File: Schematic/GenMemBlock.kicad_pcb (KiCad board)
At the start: 4 copper layers, 99.6 x 66 mm, 39 parts, among them J1 MCU_HEADER, J2 ADDR_BUS, J3 DATA_BUS, J4 CART_A20, J5 CART_B10, J6 CART_B20, J7 CART_A10, P1 MD-CART-FINGERS-doragasu, U1 74HCT595, U10 74ACT16543DL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

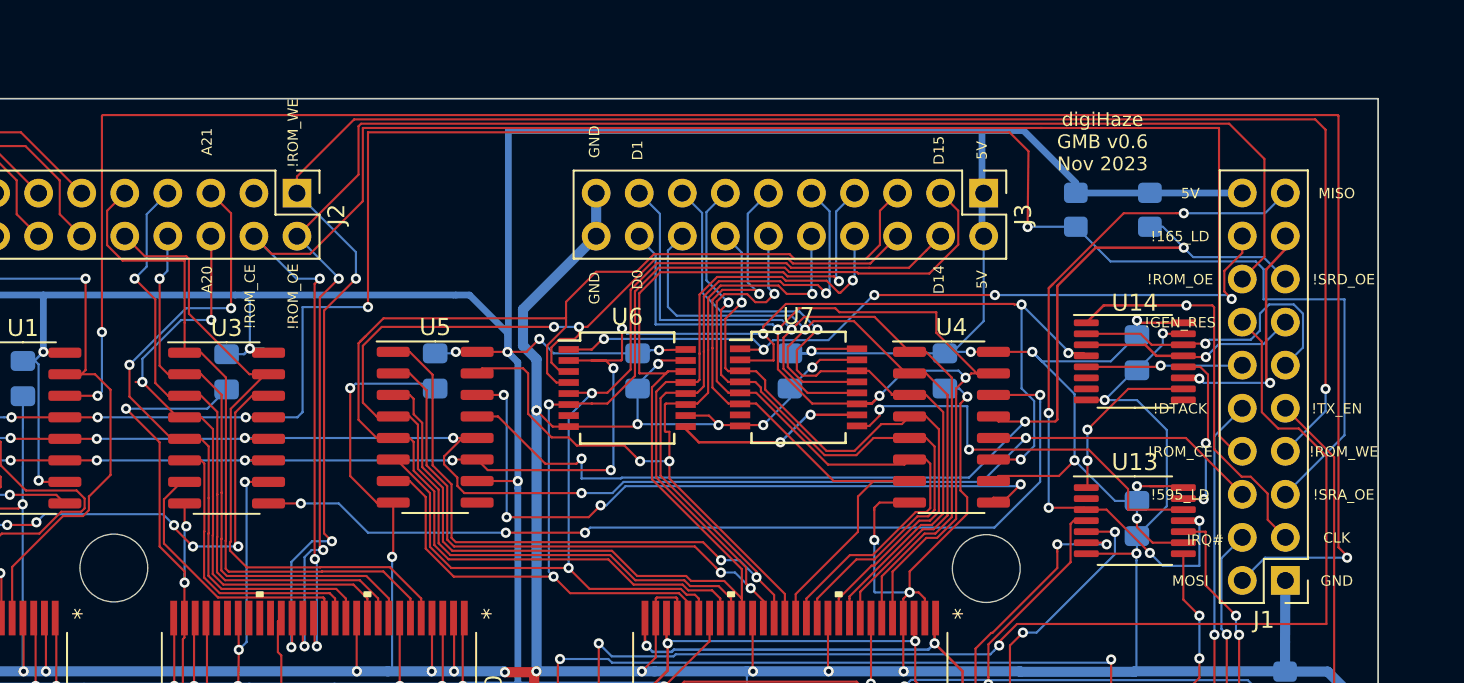
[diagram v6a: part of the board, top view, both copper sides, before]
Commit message: sdcard pinout
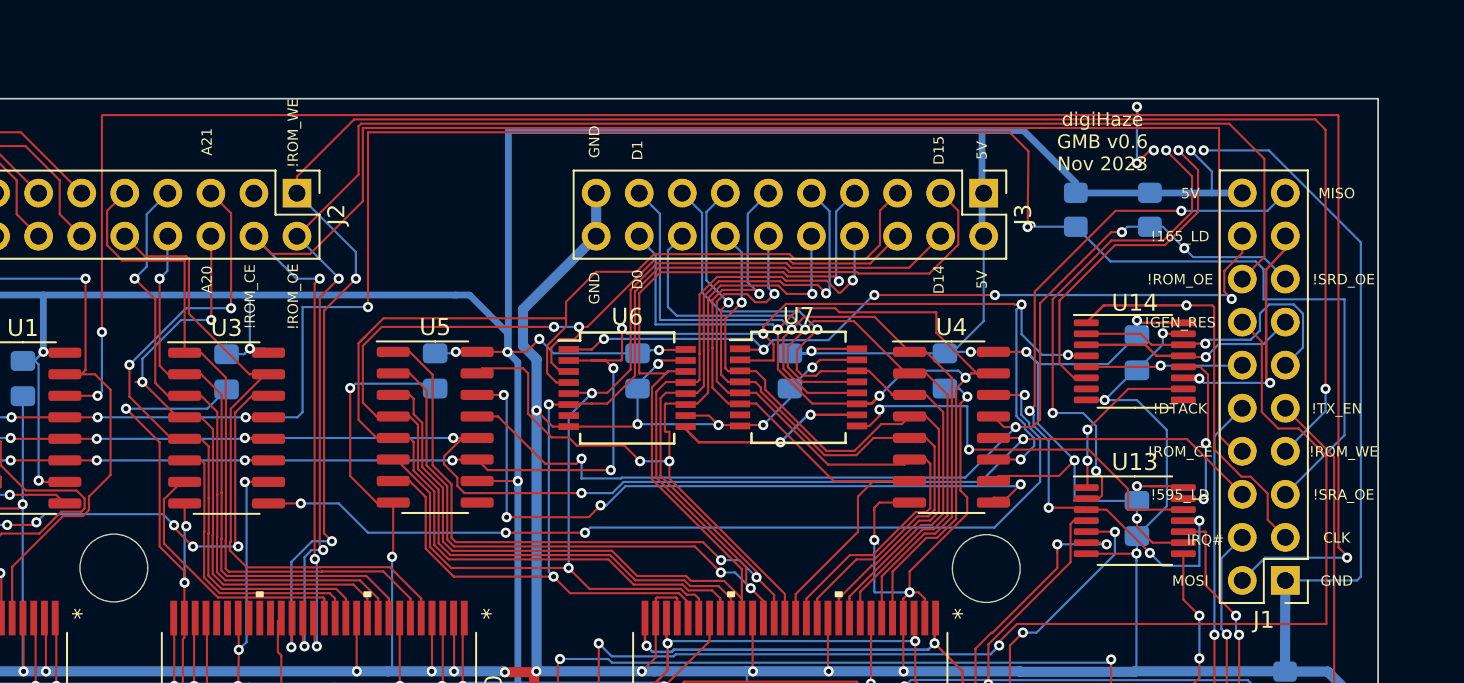
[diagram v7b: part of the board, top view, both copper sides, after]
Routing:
- net GND: track 646.6 -> 682.4 mm, vias 46 -> 47
- net SPI_MISO_SDC: track 0.00 -> 29.5 mm, vias 0 -> 3
- net CLK_SDC: track 0.00 -> 20.1 mm, vias 0 -> 1
- net /SER_MOSI: track 124.7 -> 129.8 mm, vias 3 -> 6
- net +5V: track 549.0 -> 553.7 mm, vias 40 -> 41
- net /595_DATA_OE#: track 65.6 -> 63.1 mm, vias 3 -> 4
- net MC_MISO: track 43.2 -> 44.5 mm
- net /SER_CLK: track 103.8 -> 105.0 mm

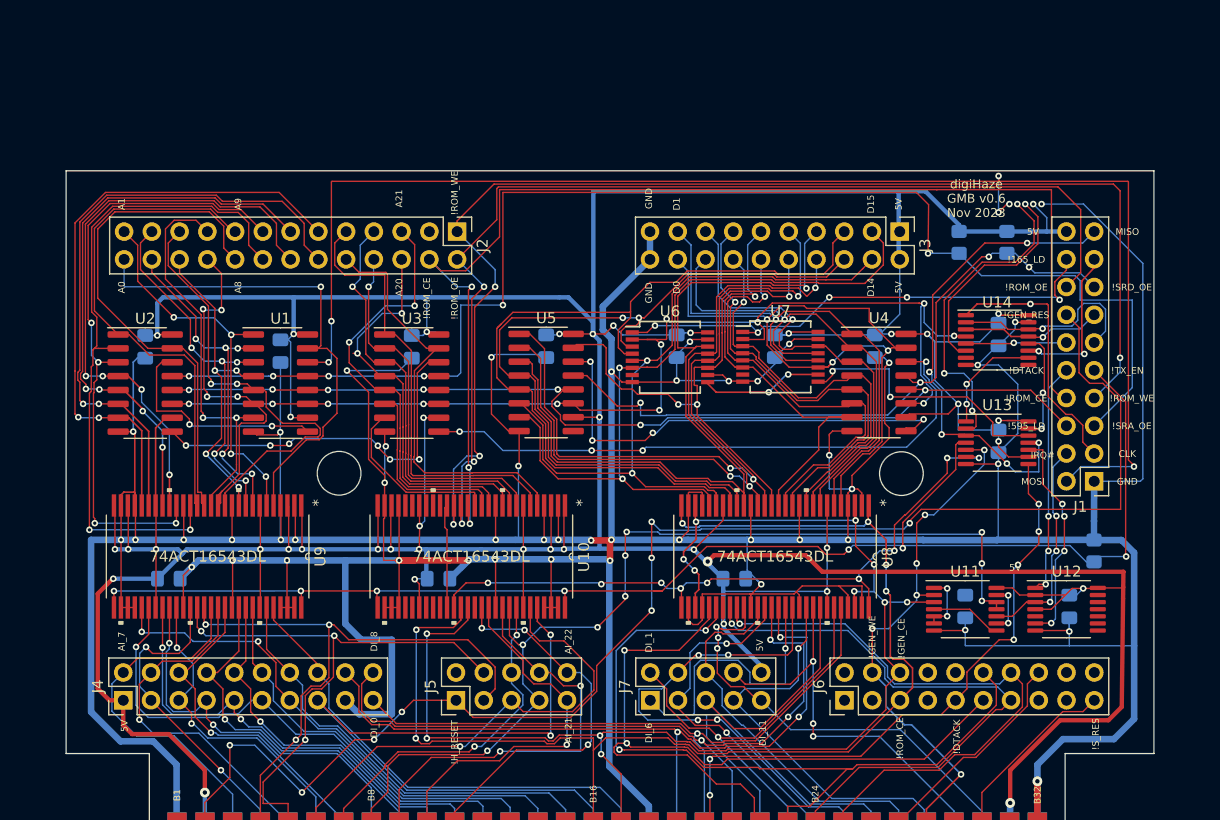
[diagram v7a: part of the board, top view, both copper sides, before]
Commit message: sdcard wiring
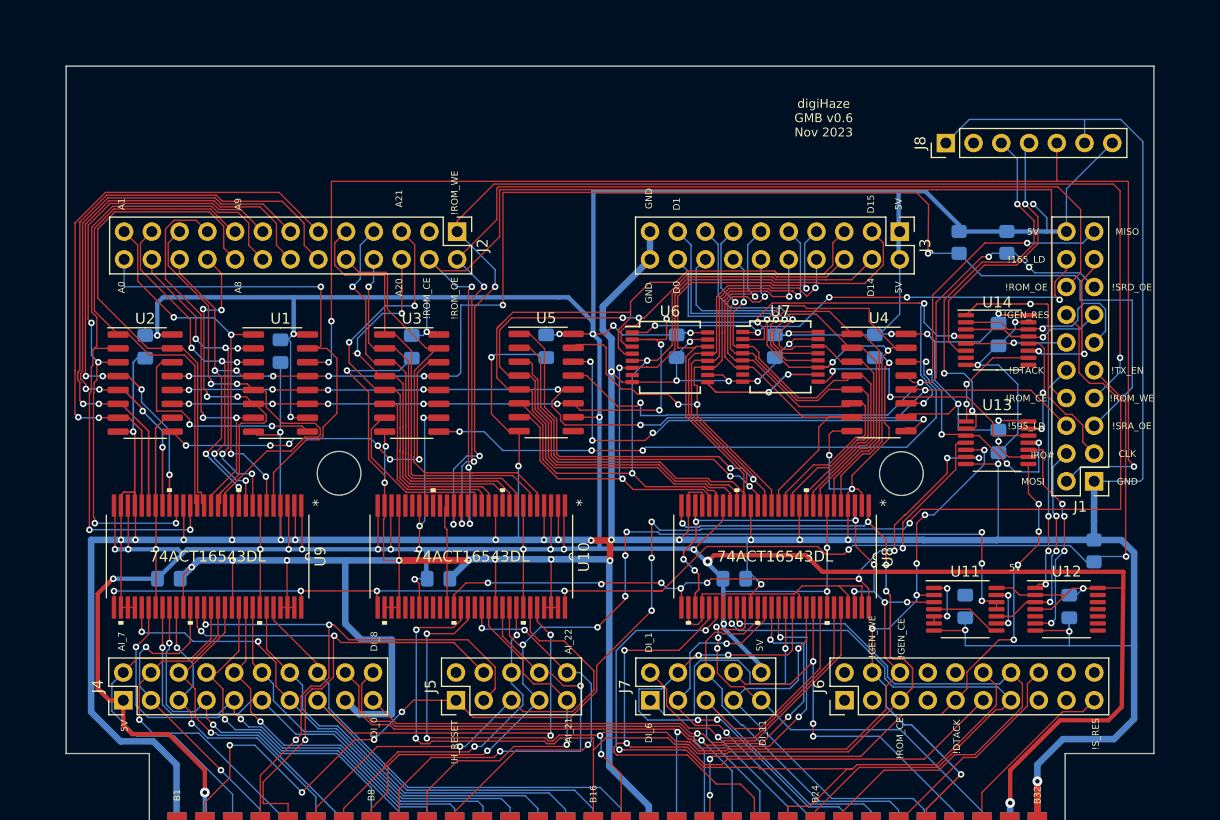
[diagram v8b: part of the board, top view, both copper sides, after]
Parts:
- added J8: SDCARD, Connector_PinHeader_2.54mm:PinHeader_1x07_P2.54mm_Vertical, F.Cu at (111.0, 66.0)
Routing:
- net GND: track 682.4 -> 703.9 mm, vias 47 -> 46
- net +5V: track 553.7 -> 563.7 mm
- net SPI_MISO_SDC: track 29.5 -> 35.6 mm
- net CLK_SDC: track 20.1 -> 25.8 mm
- net /SER_MOSI: track 129.8 -> 128.2 mm, vias 6 -> 3
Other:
- board size 99.6 x 66 mm -> 99.6 x 75.6 mm
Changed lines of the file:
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@@
     (thickness 1.6002)
     (drawings 79)
-    (tracks 3200)
+    (tracks 3204)
     (zones 0)
-    (modules 39)
-    (nets 164)
+    (modules 40)
+    (nets 165)
   )
   (page A4)
@@
   (net 162 SPI_MISO_SDC_OE#)
   (net 163 SPI_MISO_FB_OE#)
+  (net 164 "Net-(J8-Pad2)")
   (net_class Default "This is the default net class."
     (clearance 0.127)
@@
     (add_net "Net-(J6-Pad7)")
     (add_net "Net-(J6-Pad8)")
+    (add_net "Net-(J8-Pad2)")
     (add_net "Net-(P1-PadB1)")
     (add_net "Net-(P1-PadB12)")
@@
     (add_net TX_ENABLE#)
   )
+  (module Connector_PinHeader_2.54mm:PinHeader_1x07_P2.54mm_Vertical (layer Front)
+    (at 110.998 66.04 90)
+    (descr "Through hole straight pin header, 1x07, 2.54mm pitch, single row")
+    (tags "Through hole pin header THT 1x07 2.54mm single row")
+    (fp_text reference J8 (at 0 -2.33 90) (layer F.SilkS)
+      (effects (font (size 1 1) (thickness 0.15)))
+    )
+    (fp_text value SDCARD (at -2.794 1.143 180) (layer F.Fab)
+      (effects (font (size 1 1) (thickness 0.15)))
+    )
+    (fp_text user %R (at 0 7.62) (layer F.Fab)
+      (effects (font (size 1 1) (thickness 0.15)))
+    )
+    (fp_line (start -0.635 -1.27) (end 1.27 -1.27) (layer F.Fab) (width 0.1))
+    (fp_line (start 1.27 -1.27) (end 1.27 16.51) (layer F.Fab) (width 0.1))
+    (fp_line (start 1.27 16.51) (end -1.27 16.51) (layer F.Fab) (width 0.1))
+    (fp_line (start -1.27 16.51) (end -1.27 -0.635) (layer F.Fab) (width 0.1))
+    (fp_line (start -1.27 -0.635) (end -0.635 -1.27) (layer F.Fab) (width 0.1))
+    (fp_line (start -1.33 16.57) (end 1.33 16.57) (layer F.SilkS) (width 0.12))
+    (fp_line (start -1.33 1.27) (end -1.33 16.57) (layer F.SilkS) (width 0.12))
+    (fp_line (start 1.33 1.27) (end 1.33 16.57) (layer F.SilkS) (width 0.12))
+    (fp_line (start -1.33 1.27) (end 1.33 1.27) (layer F.SilkS) (width 0.12))
+    (fp_line (start -1.33 0) (end -1.33 -1.33) (layer F.SilkS) (width 0.12))
+    (fp_line (start -1.33 -1.33) (end 0 -1.33) (layer F.SilkS) (width 0.12))
+    (fp_line (start -1.8 -1.8) (end -1.8 17.05) (layer F.CrtYd) (width 0.05))
+    (fp_line (start -1.8 17.05) (end 1.8 17.05) (layer F.CrtYd) (width 0.05))
+    (fp_line (start 1.8 17.05) (end 1.8 -1.8) (layer F.CrtYd) (width 0.05))
+    (fp_line (start 1.8 -1.8) (end -1.8 -1.8) (layer F.CrtYd) (width 0.05))
+    (pad 7 thru_hole oval (at 0 15.24 90) (size 1.7 1.7) (drill 1) (layers *.Cu *.Mask)
+      (net 49 +5V))
+    (pad 6 thru_hole oval (at 0 12.7 90) (size 1.7 1.7) (drill 1) (layers *.Cu *.Mask)
+      (net 29 GND))
+    (pad 5 thru_hole oval (at 0 10.16 90) (size 1.7 1.7) (drill 1) (layers *.Cu *.Mask)
+      (net 48 /SER_MOSI))
+    (pad 4 thru_hole oval (at 0 7.62 90) (size 1.7 1.7) (drill 1) (layers *.Cu *.Mask)
+      (net 159 CLK_SDC))
+    (pad 3 thru_hole oval (at 0 5.08 90) (size 1.7 1.7) (drill 1) (layers *.Cu *.Mask)
+      (net 156 SPI_MISO_SDC))
+    (pad 2 thru_hole oval (at 0 2.54 90) (size 1.7 1.7) (drill 1) (layers *.Cu *.Mask)
+      (net 164 "Net-(J8-Pad2)"))
+    (pad 1 thru_hole rect (at 0 0 90) (size 1.7 1.7) (drill 1) (layers *.Cu *.Mask)
+      (net 29 GND))
+    (model ${KISYS3DMOD}/Connector_PinHeader_2.54mm.3dshapes/PinHeader_1x07_P2.54mm_Vertical.wrl
+      (at (xyz 0 0 0))
+      (scale (xyz 1 1 1))
+      (rotate (xyz 0 0 0))
+    )
+  )
   (module Connector_PinHeader_2.54mm:PinHeader_2x10_P2.54mm_Vertical (layer Front)
     (at 124.577 97 180)
@@
     )
   )
-  (gr_text "digiHaze\nGMB v0.6\nNov 2023" (at 113.792 71.12) (layer F.SilkS)
+  (gr_text "digiHaze\nGMB v0.6\nNov 2023" (at 99.822 63.754) (layer F.SilkS)
     (effects (font (size 0.8128 0.8128) (thickness 0.1524)))
   )
@@
     (effects (font (size 0.6128 0.6128) (thickness 0.1524)))
   )
-  (gr_line (start 30.48 68.58) (end 130.048 68.58) (layer Edge.Cuts) (width 0.1))
-  (gr_line (start 130.048 68.58) (end 130.048 121.92) (layer Edge.Cuts) (width 0.1))
-  (gr_line (start 30.48 121.92) (end 30.48 68.58) (layer Edge.Cuts) (width 0.1))
+  (gr_line (start 30.48 59) (end 130.048 59) (layer Edge.Cuts) (width 0.1))
+  (gr_line (start 130.048 59) (end 130.048 121.92) (layer Edge.Cuts) (width 0.1))
+  (gr_line (start 30.48 121.92) (end 30.48 59) (layer Edge.Cuts) (width 0.1))
   (dimension 0.127 (width 0.1524) (layer Cmts.User)
     (gr_text "0.127 mm" (at 78.7908 118.4275 90) (layer Cmts.User)
@@
   (segment (start 105.41 86.563198) (end 105.41 91.69506) (width 0.127) (layer Front) (net 29))
   (segment (start 105.8164 86.156798) (end 105.41 86.563198) (width 0.127) (layer Front) (net 29))
-  (segment (start 124.577 97) (end 128.806 97) (width 0.127) (layer Back) (net 29))
+  (segment (start 113.157 63.881) (end 110.998 66.04) (width 0.127) (layer Back) (net 29))
+  (segment (start 129.032 65.913) (end 127 63.881) (width 0.127) (layer Back) (net 29))
+  (segment (start 129.032 96.774) (end 129.032 65.913) (width 0.127) (layer Back) (net 29))
   (segment (start 128.806 97) (end 129.032 96.774) (width 0.127) (layer Back) (net 29))
-  (segment (start 123.604942 71.628) (end 119.761 71.628) (width 0.127) (layer Back) (net 29))
-  (segment (start 129.032 77.055058) (end 123.604942 71.628) (width 0.127) (layer Back) (net 29))
-  (via (at 119.761 71.628) (size 0.6) (drill 0.3) (layers Front Back) (net 29))
-  (segment (start 129.032 96.774) (end 129.032 77.055058) (width 0.127) (layer Back) (net 29))
+  (segment (start 124.577 97) (end 128.806 97) (width 0.127) (layer Back) (net 29))
+  (segment (start 123.698 66.04) (end 123.698 63.881) (width 0.127) (layer Back) (net 29))
+  (segment (start 123.698 63.881) (end 113.157 63.881) (width 0.127) (layer Back) (net 29))
+  (segment (start 127 63.881) (end 123.698 63.881) (width 0.127) (layer Back) (net 29))
+  (segment (start 126.365 66.167) (end 126.238 66.04) (width 0.127) (layer Back) (net 49))
   (segment (start 81.5848 112.4712) (end 81.5848 112.4712) (width 0.127) (layer Front) (net 30))
   (via (at 81.5848 112.4712) (size 0.6) (drill 0.3) (layers Front Back) (net 30))
@@
   (segment (start 54.7624 85.852) (end 54.5084 86.106) (width 0.127) (layer Back) (net 48))
   (segment (start 54.7624 82.3468) (end 54.7624 85.852) (width 0.127) (layer Back) (net 48))
-  (via (at 115.824 69.057) (size 0.6) (drill 0.3) (layers Front Back) (net 48))
-  (segment (start 115.87481 69.10781) (end 115.824 69.057) (width 0.127) (layer Front) (net 48))
-  (segment (start 115.87481 69.54519) (end 115.87481 69.10781) (width 0.127) (layer Front) (net 48))
   (segment (start 54.81321 69.54519) (end 115.87481 69.54519) (width 0.127) (layer Front) (net 48))
-  (segment (start 115.87481 69.54519) (end 127.664014 69.54519) (width 0.127) (layer Front) (net 48))
-  (via (at 115.824 72.39) (size 0.6) (drill 0.3) (layers Front Back) (net 48))
-  (segment (start 115.824 69.057) (end 115.824 72.39) (width 0.127) (layer Back) (net 48))
-  (segment (start 115.824 72.39) (end 116.585982 71.628018) (width 0.127) (layer Front) (net 48))
-  (segment (start 116.585982 71.628018) (end 116.817963 71.628018) (width 0.127) (layer Front) (net 48))
-  (via (at 116.817963 71.628018) (size 0.6) (drill 0.3) (layers Front Back) (net 48))
+  (segment (start 121.158 66.04) (end 121.158 69.469) (width 0.127) (layer Front) (net 48))
+  (segment (start 121.23419 69.54519) (end 127.664014 69.54519) (width 0.127) (layer Front) (net 48))
+  (segment (start 121.158 69.469) (end 121.23419 69.54519) (width 0.127) (layer Front) (net 48))
+  (segment (start 115.87481 69.54519) (end 121.23419 69.54519) (width 0.127) (layer Front) (net 48))
   (segment (start 50.1015 84.0525) (end 50.7707 84.0525) (width 0.15) (layer Back) (net 49))
   (segment (start 50.7707 84.0525) (end 51.308 83.5152) (width 0.15) (layer Back) (net 49))
@@
   (via (at 118.999 71.628) (size 0.6) (drill 0.3) (layers Front Back) (net 49))
   (segment (start 120.241 72.87) (end 118.999 71.628) (width 0.127) (layer Back) (net 49))
+  (segment (start 122.037 70.241) (end 126.238 66.04) (width 0.127) (layer Back) (net 49))
+  (segment (start 122.037 74.14) (end 122.037 70.241) (width 0.127) (layer Back) (net 49))
   (segment (start 41.8084 87.376) (end 41.8084 87.376) (width 0.127) (layer Front) (net 50))
   (segment (start 49.4284 87.376) (end 49.4284 87.376) (width 0.127) (layer Back) (net 50))
@@
   (segment (start 119.075191 73.158217) (end 117.544974 71.628) (width 0.127) (layer Front) (net 156))
   (segment (start 110.8535 87.122) (end 110.8535 80.4085) (width 0.127) (layer Front) (net 156))
+  (segment (start 117.544974 67.506974) (end 116.078 66.04) (width 0.127) (layer Back) (net 156))
+  (segment (start 117.544974 71.628) (end 117.544974 67.506974) (width 0.127) (layer Back) (net 156))
   (segment (start 114.532224 77.216) (end 117.475 77.216) (width 0.127) (layer Front) (net 159))
   (segment (start 111.252 80.496224) (end 114.532224 77.216) (width 0.127) (layer Front) (net 159))
@@
   (segment (start 119.425999 75.265001) (end 119.425999 72.782012) (width 0.127) (layer Front) (net 159))
   (via (at 118.271987 71.628) (size 0.6) (drill 0.3) (layers Front Back) (net 159))
+  (segment (start 118.271987 66.386013) (end 118.618 66.04) (width 0.127) (layer Back) (net 159))
+  (segment (start 118.271987 71.628) (end 118.271987 66.386013) (width 0.127) (layer Back) (net 159))
   (via (at 119.507 93.472) (size 0.6) (drill 0.3) (layers Front Back) (net 160))
   (segment (start 119.507 93.472) (end 119.582224 93.472) (width 0.127) (layer Front) (net 160))
